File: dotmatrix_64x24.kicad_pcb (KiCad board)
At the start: 2 copper layers, 180 x 100 mm, 146 parts, among them CON1 BARREL_JACK, CON2 MRUSB-2B, P1 CONN_01X09, P2 CONN_01X09, P3 CONN_01X04, P4 CONN_01X03, P6 CONN_01X03, Q1 NJL7302L-F3, SW1 SW_PUSH_SMALL_H, SW2 SW_PUSH_SMALL_H, SW3 SW_PUSH_SMALL_H, SW4 SW_PUSH_SMALL_H, SW5 SW_PUSH_SMALL_H, SW6 SW_PUSH_SMALL_H, SW7 SW_PUSH_SMALL_H, SW8 SW_PUSH_SMALL_H, U1 WROOM-02, U10 LED1642GW, U11 LED1642GW, U12 AE-BME280, U13 OKL-T/6-W5, U14 NJU7223, U15 DS1307, U2 74HC595-alt-vdd, U3 TD62783, U4 74HC595-alt-vdd, U5 TD62783, U6 LED1642GW, U7 74HC595-alt-vdd, U8 TD62783, U9 LED1642GW, Y1 Crystal_Small

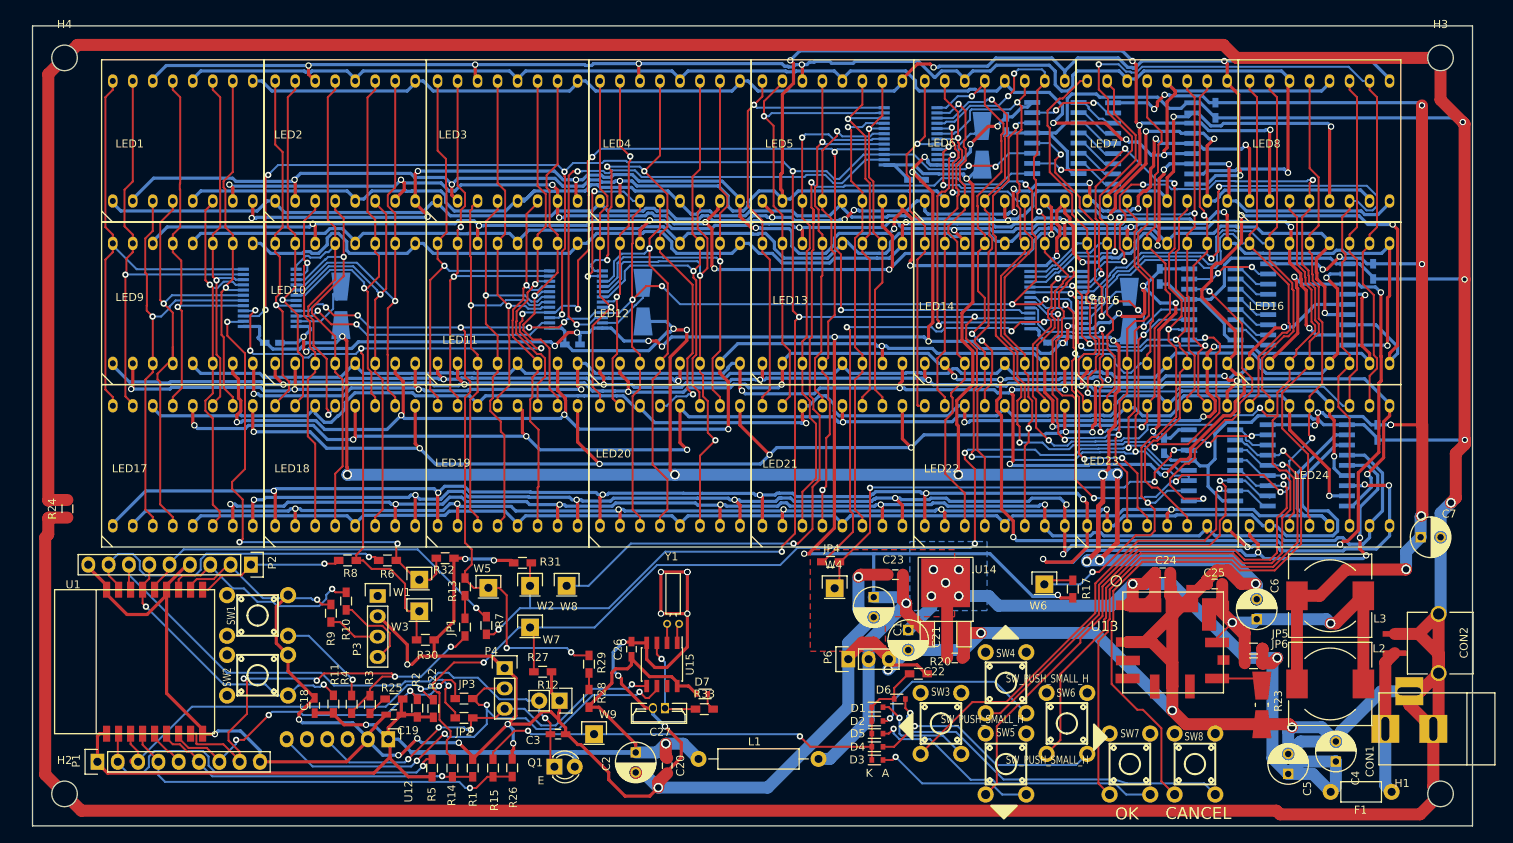
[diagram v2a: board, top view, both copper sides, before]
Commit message: Added CH340G USB-to-Serial chip
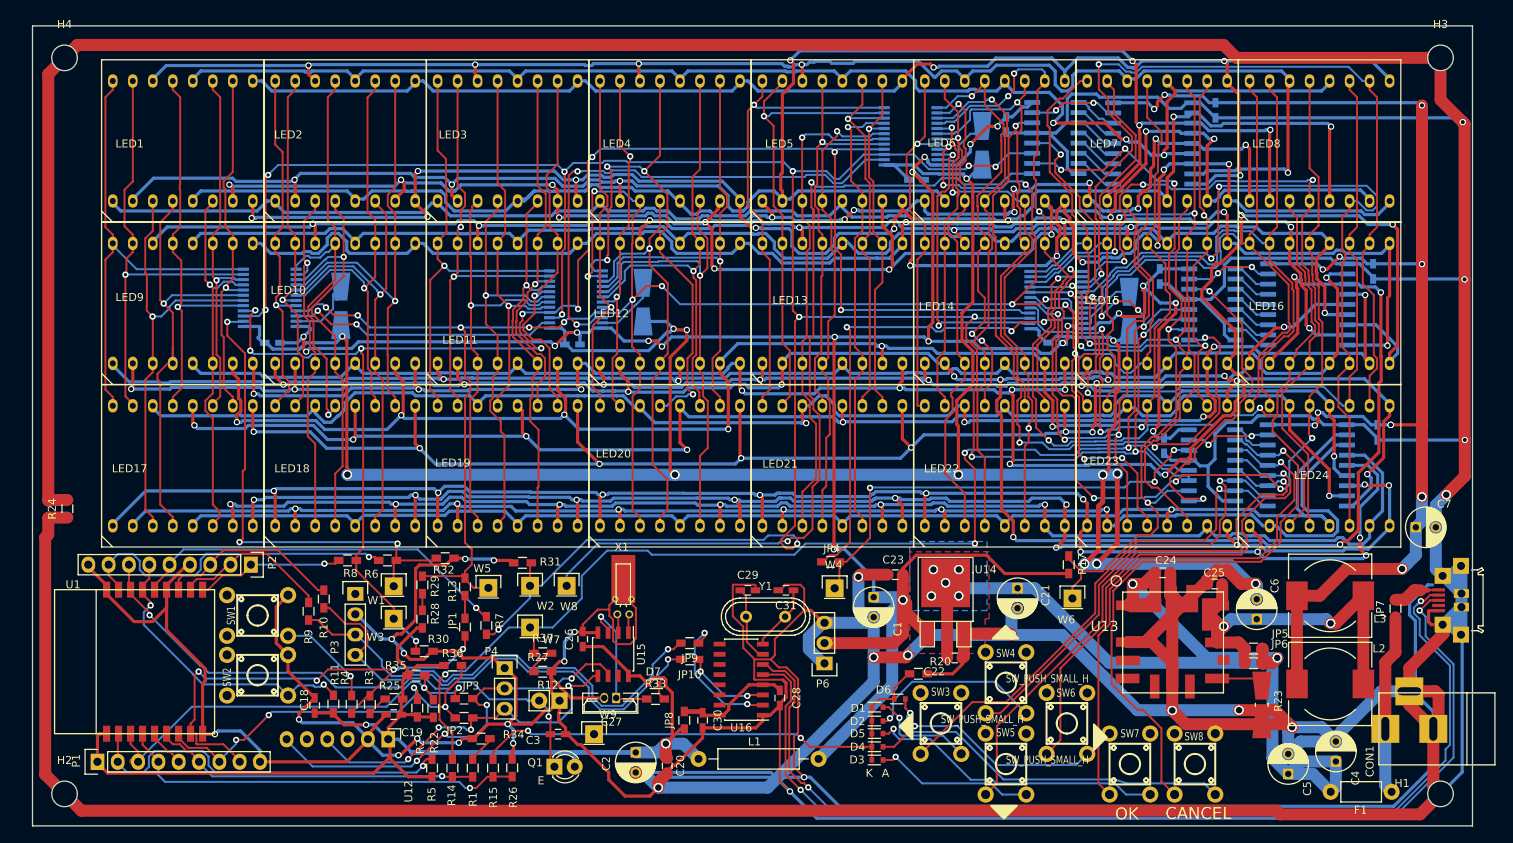
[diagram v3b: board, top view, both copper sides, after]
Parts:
- removed CON2: MRUSB-2B, components:MRUSB-2B
- added C28: 1u, Capacitors_SMD:C_0603_HandSoldering, F.Cu at (105.4, 96.0)
- added C29: 22p, Capacitors_SMD:C_0603_HandSoldering, F.Cu at (101.4, 82.5)
- added C30: 1u, Capacitors_SMD:C_0603_HandSoldering, F.Cu at (95.8, 98.8)
- added C31: 22p, Capacitors_SMD:C_0603_HandSoldering, F.Cu at (106.2, 82.5)
- added JP10: Jumper_NC_Small, Resistors_SMD:R_0603_HandSoldering, F.Cu at (94.2, 91.2)
- added JP7: Jumper_NC_Small, Resistors_SMD:R_0603_HandSoldering, F.Cu at (182.4, 84.8)
- added JP8: Jumper_NC_Small, Resistors_SMD:R_0603_HandSoldering, F.Cu at (93.5, 98.8)
- added JP9: Jumper_NC_Small, Resistors_SMD:R_0603_HandSoldering, F.Cu at (94.2, 89.2)
- added P5: USB_OTG, components:ZX62R-B-5P, F.Cu at (190.6, 83.8)
- added R34: 10k, Resistors_SMD:R_0603_HandSoldering, F.Cu at (68.1, 101.1)
- added R35: 10k, Resistors_SMD:R_0603_HandSoldering, F.Cu at (59.9, 93.2)
- added R36: 10k, Resistors_SMD:R_0603_HandSoldering, F.Cu at (64.5, 91.9)
- added R37: 10k, Resistors_SMD:R_0603_HandSoldering, F.Cu at (75.8, 90.4)
- added U16: CH340G, Housings_SOIC:SOIC-16_3.9x9.9mm_Pitch1.27mm, F.Cu at (100.6, 93.7)
- added X1: CRYSTAL_SMD, components:Crystal_Round_Horizontal_2mm_SHIELD, F.Cu at (85.9, 85.6)
- Y1: value Crystal_Small -> 12MHz; footprint Crystals:Crystal_Round_Horizontal_2mm -> Crystals:Crystal_HC49-U_Vertical
- moved R29 23.1 mm to (60.7, 81.9)
- moved R28 23.1 mm to (60.7, 86.2)
- moved C21 14.6 mm to (135.1, 82.3)
- moved Y1 11.6 mm to (103.6, 85.9)
- moved D7 6.23 mm to (89.6, 94.2)
- moved C27 6.23 mm to (85.0, 96.0)
- moved U15 6.23 mm to (84.6, 90.6)
- moved R33 6.23 mm to (89.9, 96.1)
- moved C26 6.23 mm to (80.8, 88.6)
- moved W6 3.92 mm to (142.0, 83.6)
- moved W3 3.33 mm to (57.1, 86.1)
- moved W1 3.30 mm to (57.1, 82.0)
- moved R17 3.09 mm to (141.5, 79.4)
- moved P6 3.02 mm to (111.0, 91.7), turned to 180 degrees
- moved P3 2.81 mm to (52.3, 83.0)
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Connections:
- net Net-(P3-Pad3) renamed /RXD
- net Net-(P3-Pad4) renamed /TXD
- P1 pad 3: Net-(JP2-Pad1) -> Net-(JP3-Pad1)
- P1 pad 7: Net-(JP3-Pad1) -> Net-(JP2-Pad1)
- R1 pad 1: GND -> Net-(R1-Pad1)
- R2 pad 2: Net-(JP3-Pad1) -> Net-(JP2-Pad1)
- R22 pad 2: Net-(JP2-Pad1) -> Net-(JP3-Pad1)
- R27 pad 1: /Sheet57A04605/HC595LATCH -> Net-(R27-Pad1)
- U1 pad 3: Net-(JP2-Pad1) -> Net-(JP3-Pad1)
- U1 pad 7: Net-(JP3-Pad1) -> Net-(JP2-Pad1)
- Y1 pad 1: Net-(U15-Pad2) -> Net-(C29-Pad1)
- Y1 pad 2: Net-(U15-Pad1) -> Net-(C31-Pad1)
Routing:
- net GND: track 1520.8 -> 1896.1 mm, vias 41 -> 40
- net /USB_DM: track 0.00 -> 128.0 mm, vias 0 -> 2
- net /USB_DP: track 0.00 -> 127.3 mm, vias 0 -> 2
- net /RXD: track 6.60 -> 59.5 mm, vias 0 -> 1
- net /TXD: track 10.3 -> 60.9 mm, vias 0 -> 1
- net VCC: track 119.9 -> 140.0 mm
- net Net-(JP9-Pad1): track 0.00 -> 17.4 mm, vias 0 -> 2
- net /Sheet57A04605/COLPWCLK: track 195.1 -> 180.6 mm, vias 14 -> 12
- net Net-(C28-Pad1): track 0.00 -> 14.3 mm
- net /ESPVDD: track 144.1 -> 157.1 mm
- net /Sheet57A04605/r21: track 220.3 -> 209.1 mm
- net Net-(JP10-Pad1): track 0.00 -> 10.7 mm, vias 0 -> 2
- net /SCL: track 64.2 -> 53.7 mm
- net Net-(C29-Pad1): track 0.00 -> 9.43 mm
- net Net-(JP3-Pad1): track 44.6 -> 54.0 mm, vias 4 -> 2
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
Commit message: filled copper zones, placed via stitching ... etc.
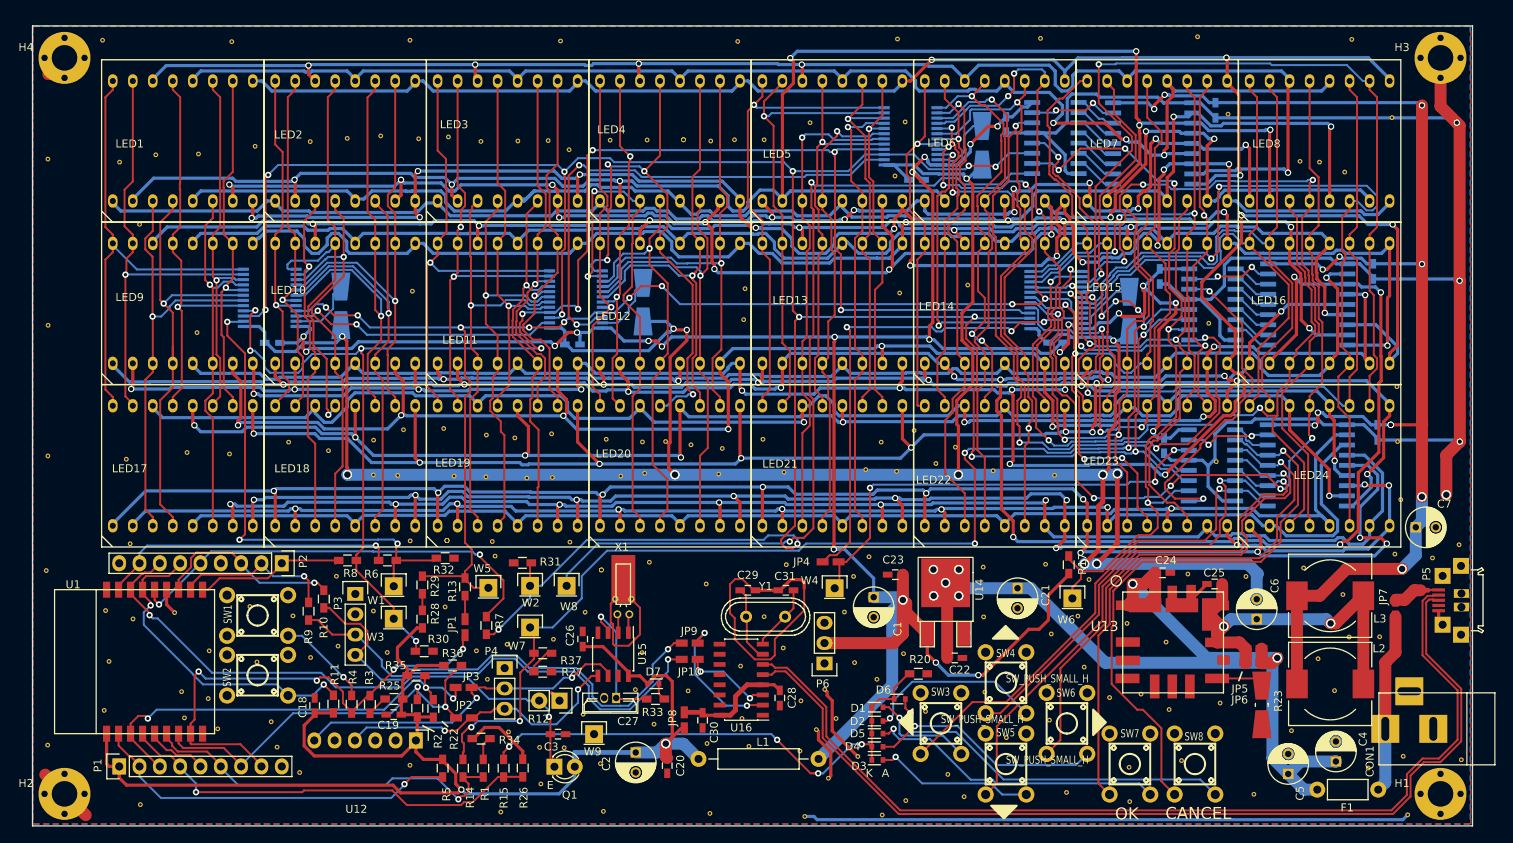
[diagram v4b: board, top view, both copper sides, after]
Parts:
- removed R24: 120R, Resistors_SMD:R_0603_HandSoldering
- added REF**: stitch-via-0.6mm, components:stitch-via-0.6mm, F.Cu at (108.1, 96.4)
- added REF**: stitch-via-0.6mm, components:stitch-via-0.6mm, F.Cu at (116.2, 67.5)
- added REF**: stitch-via-0.6mm, components:stitch-via-0.6mm, F.Cu at (71.5, 100.3)
- added REF**: stitch-via-0.6mm, components:stitch-via-0.6mm, F.Cu at (68.9, 93.7)
- added REF**: stitch-via-0.6mm, components:stitch-via-0.6mm, F.Cu at (54.6, 85.1)
- added REF**: stitch-via-0.6mm, components:stitch-via-0.6mm, F.Cu at (50.0, 80.8)
- added REF**: stitch-via-0.6mm, components:stitch-via-0.6mm, F.Cu at (50.2, 89.5)
- added REF**: stitch-via-0.6mm, components:stitch-via-0.6mm, F.Cu at (46.8, 91.0)
- added REF**: stitch-via-0.6mm, components:stitch-via-0.6mm, F.Cu at (59.2, 104.4)
- added REF**: stitch-via-0.6mm, components:stitch-via-0.6mm, F.Cu at (45.4, 105.3)
- added REF**: stitch-via-0.6mm, components:stitch-via-0.6mm, F.Cu at (42.6, 102.2)
- added REF**: stitch-via-0.6mm, components:stitch-via-0.6mm, F.Cu at (41.8, 99.0)
- added REF**: stitch-via-0.6mm, components:stitch-via-0.6mm, F.Cu at (105.9, 67.8)
- added REF**: stitch-via-0.6mm, components:stitch-via-0.6mm, F.Cu at (35.2, 99.9)
- added REF**: stitch-via-0.6mm, components:stitch-via-0.6mm, F.Cu at (39.2, 84.6)
- added REF**: stitch-via-0.6mm, components:stitch-via-0.6mm, F.Cu at (29.8, 85.3)
- added REF**: stitch-via-0.6mm, components:stitch-via-0.6mm, F.Cu at (21.0, 97.6)
- added REF**: stitch-via-0.6mm, components:stitch-via-0.6mm, F.Cu at (21.1, 85.1)
- added REF**: stitch-via-0.6mm, components:stitch-via-0.6mm, F.Cu at (13.9, 101.9)
- added REF**: stitch-via-0.6mm, components:stitch-via-0.6mm, F.Cu at (159.0, 49.2)
- added REF**: stitch-via-0.6mm, components:stitch-via-0.6mm, F.Cu at (160.0, 66.5)
- added REF**: stitch-via-0.6mm, components:stitch-via-0.6mm, F.Cu at (120.0, 67.7)
- added REF**: stitch-via-0.6mm, components:stitch-via-0.6mm, F.Cu at (122.2, 62.6)
- added REF**: stitch-via-0.6mm, components:stitch-via-0.6mm, F.Cu at (97.8, 68.0)
- added REF**: stitch-via-0.6mm, components:stitch-via-0.6mm, F.Cu at (128.9, 44.4)
- added REF**: stitch-via-0.6mm, components:stitch-via-0.6mm, F.Cu at (100.9, 48.7)
- added REF**: stitch-via-0.6mm, components:stitch-via-0.6mm, F.Cu at (103.5, 26.2)
- added REF**: stitch-via-0.6mm, components:stitch-via-0.6mm, F.Cu at (99.7, 26.2)
- added REF**: stitch-via-0.6mm, components:stitch-via-0.6mm, F.Cu at (96.8, 26.4)
- added REF** (x2): stitch-via-0.6mm, components:stitch-via-0.6mm, F.Cu at (93.4, 26.2)
- added REF**: stitch-via-0.6mm, components:stitch-via-0.6mm, F.Cu at (88.8, 26.3)
- added REF**: stitch-via-0.6mm, components:stitch-via-0.6mm, F.Cu at (84.2, 26.3)
- added REF**: stitch-via-0.6mm, components:stitch-via-0.6mm, F.Cu at (79.1, 27.5)
- added REF**: stitch-via-0.6mm, components:stitch-via-0.6mm, F.Cu at (88.5, 67.9)
- added REF**: stitch-via-0.6mm, components:stitch-via-0.6mm, F.Cu at (76.5, 26.3)
- added REF**: stitch-via-0.6mm, components:stitch-via-0.6mm, F.Cu at (72.7, 26.4)
- added REF**: stitch-via-0.6mm, components:stitch-via-0.6mm, F.Cu at (68.0, 26.4)
- added REF**: stitch-via-0.6mm, components:stitch-via-0.6mm, F.Cu at (64.0, 25.9)
- added REF**: stitch-via-0.6mm, components:stitch-via-0.6mm, F.Cu at (60.3, 26.1)
- added REF**: stitch-via-0.6mm, components:stitch-via-0.6mm, F.Cu at (55.5, 25.8)
- added REF**: stitch-via-0.6mm, components:stitch-via-0.6mm, F.Cu at (51.3, 26.1)
- added REF**: stitch-via-0.6mm, components:stitch-via-0.6mm, F.Cu at (46.7, 26.5)
- added REF**: stitch-via-0.6mm, components:stitch-via-0.6mm, F.Cu at (39.8, 27.1)
- added REF**: stitch-via-0.6mm, components:stitch-via-0.6mm, F.Cu at (32.7, 28.0)
- added REF**: stitch-via-0.6mm, components:stitch-via-0.6mm, F.Cu at (85.5, 68.3)
- added REF**: stitch-via-0.6mm, components:stitch-via-0.6mm, F.Cu at (27.4, 28.1)
- added REF**: stitch-via-0.6mm, components:stitch-via-0.6mm, F.Cu at (22.9, 29.0)
- added REF**: stitch-via-0.6mm, components:stitch-via-0.6mm, F.Cu at (25.4, 36.8)
- added REF**: stitch-via-0.6mm, components:stitch-via-0.6mm, F.Cu at (32.6, 50.3)
- added REF**: stitch-via-0.6mm, components:stitch-via-0.6mm, F.Cu at (23.7, 66.2)
- added REF**: stitch-via-0.6mm, components:stitch-via-0.6mm, F.Cu at (31.3, 65.3)
- added REF**: stitch-via-0.6mm, components:stitch-via-0.6mm, F.Cu at (36.6, 65.5)
- added REF**: stitch-via-0.6mm, components:stitch-via-0.6mm, F.Cu at (44.0, 64.0)
- added REF**: stitch-via-0.6mm, components:stitch-via-0.6mm, F.Cu at (49.0, 65.1)
- added REF**: stitch-via-0.6mm, components:stitch-via-0.6mm, F.Cu at (54.6, 63.8)
- added REF**: stitch-via-0.6mm, components:stitch-via-0.6mm, F.Cu at (77.0, 68.5)
- added REF**: stitch-via-0.6mm, components:stitch-via-0.6mm, F.Cu at (58.4, 62.5)
- added REF**: stitch-via-0.6mm, components:stitch-via-0.6mm, F.Cu at (63.4, 62.3)
- added REF**: stitch-via-0.6mm, components:stitch-via-0.6mm, F.Cu at (68.7, 63.1)
- added REF**: stitch-via-0.6mm, components:stitch-via-0.6mm, F.Cu at (72.3, 63.5)
- added REF**: stitch-via-0.6mm, components:stitch-via-0.6mm, F.Cu at (76.9, 63.0)
- added REF**: stitch-via-0.6mm, components:stitch-via-0.6mm, F.Cu at (83.7, 63.7)
- added REF**: stitch-via-0.6mm, components:stitch-via-0.6mm, F.Cu at (88.2, 64.0)
- added REF**: stitch-via-0.6mm, components:stitch-via-0.6mm, F.Cu at (91.1, 64.0)
- added REF**: stitch-via-0.6mm, components:stitch-via-0.6mm, F.Cu at (94.3, 64.4)
- added REF**: stitch-via-0.6mm, components:stitch-via-0.6mm, F.Cu at (98.2, 64.8)
- added REF**: stitch-via-0.6mm, components:stitch-via-0.6mm, F.Cu at (73.8, 68.5)
- added REF**: stitch-via-0.6mm, components:stitch-via-0.6mm, F.Cu at (103.3, 63.7)
- added REF**: stitch-via-0.6mm, components:stitch-via-0.6mm, F.Cu at (118.1, 64.0)
- added REF**: stitch-via-0.6mm, components:stitch-via-0.6mm, F.Cu at (120.4, 45.4)
- added REF**: stitch-via-0.6mm, components:stitch-via-0.6mm, F.Cu at (101.1, 44.9)
- added REF**: stitch-via-0.6mm, components:stitch-via-0.6mm, F.Cu at (59.5, 45.2)
- added REF**: stitch-via-0.6mm, components:stitch-via-0.6mm, F.Cu at (109.2, 24.1)
- added REF**: stitch-via-0.6mm, components:stitch-via-0.6mm, F.Cu at (119.8, 30.8)
- added REF**: stitch-via-0.6mm, components:stitch-via-0.6mm, F.Cu at (170.4, 28.9)
- added REF**: stitch-via-0.6mm, components:stitch-via-0.6mm, F.Cu at (161.4, 23.0)
- added REF**: stitch-via-0.6mm, components:stitch-via-0.6mm, F.Cu at (176.0, 30.3)
- added REF**: stitch-via-0.6mm, components:stitch-via-0.6mm, F.Cu at (68.7, 68.4)
- added REF**: stitch-via-0.6mm, components:stitch-via-0.6mm, F.Cu at (172.9, 29.0)
- added REF**: stitch-via-0.6mm, components:stitch-via-0.6mm, F.Cu at (181.9, 23.5)
- added REF**: stitch-via-0.6mm, components:stitch-via-0.6mm, F.Cu at (182.5, 57.1)
- added REF**: stitch-via-0.6mm, components:stitch-via-0.6mm, F.Cu at (182.6, 64.0)
- added REF**: stitch-via-0.6mm, components:stitch-via-0.6mm, F.Cu at (183.0, 71.2)
- added REF**: stitch-via-0.6mm, components:stitch-via-0.6mm, F.Cu at (187.0, 78.5)
- added REF**: stitch-via-0.6mm, components:stitch-via-0.6mm, F.Cu at (190.3, 76.9)
- added REF**: stitch-via-0.6mm, components:stitch-via-0.6mm, F.Cu at (175.8, 83.1)
- added REF**: stitch-via-0.6mm, components:stitch-via-0.6mm, F.Cu at (176.6, 88.4)
- added REF**: stitch-via-0.6mm, components:stitch-via-0.6mm, F.Cu at (183.3, 103.3)
- added REF**: stitch-via-0.6mm, components:stitch-via-0.6mm, F.Cu at (64.7, 68.3)
- added REF**: stitch-via-0.6mm, components:stitch-via-0.6mm, F.Cu at (190.6, 103.7)
- added REF**: stitch-via-0.6mm, components:stitch-via-0.6mm, F.Cu at (183.9, 110.6)
- added REF**: stitch-via-0.6mm, components:stitch-via-0.6mm, F.Cu at (176.9, 13.7)
- added REF**: stitch-via-0.6mm, components:stitch-via-0.6mm, F.Cu at (157.6, 13.4)
- added REF**: stitch-via-0.6mm, components:stitch-via-0.6mm, F.Cu at (138.0, 13.6)
- added REF**: stitch-via-0.6mm, components:stitch-via-0.6mm, F.Cu at (120.1, 13.6)
- added REF**: stitch-via-0.6mm, components:stitch-via-0.6mm, F.Cu at (100.2, 13.9)
- added REF**: stitch-via-0.6mm, components:stitch-via-0.6mm, F.Cu at (78.0, 13.9)
- added REF**: stitch-via-0.6mm, components:stitch-via-0.6mm, F.Cu at (59.2, 13.8)
- added REF**: stitch-via-0.6mm, components:stitch-via-0.6mm, F.Cu at (36.9, 14.0)
- added REF**: stitch-via-0.6mm, components:stitch-via-0.6mm, F.Cu at (54.6, 68.1)
- added REF**: stitch-via-0.6mm, components:stitch-via-0.6mm, F.Cu at (20.8, 13.8)
- added REF**: stitch-via-0.6mm, components:stitch-via-0.6mm, F.Cu at (13.9, 28.7)
- added REF**: stitch-via-0.6mm, components:stitch-via-0.6mm, F.Cu at (13.9, 49.4)
- added REF**: stitch-via-0.6mm, components:stitch-via-0.6mm, F.Cu at (13.9, 65.8)
- added REF**: stitch-via-0.6mm, components:stitch-via-0.6mm, F.Cu at (59.2, 76.4)
- added REF**: stitch-via-0.6mm, components:stitch-via-0.6mm, F.Cu at (25.5, 109.3)
- added REF**: stitch-via-0.6mm, components:stitch-via-0.6mm, F.Cu at (13.7, 80.1)
- added REF**: stitch-via-0.6mm, components:stitch-via-0.6mm, F.Cu at (44.6, 85.8)
- added REF**: stitch-via-0.6mm, components:stitch-via-0.6mm, F.Cu at (63.6, 84.6)
- added REF** (x2): stitch-via-0.6mm, components:stitch-via-0.6mm, F.Cu at (83.1, 80.0)
- added REF**: stitch-via-0.6mm, components:stitch-via-0.6mm, F.Cu at (141.2, 107.8)
- added REF**: stitch-via-0.6mm, components:stitch-via-0.6mm, F.Cu at (57.7, 68.2)
- added REF**: stitch-via-0.6mm, components:stitch-via-0.6mm, F.Cu at (89.1, 79.0)
- added REF**: stitch-via-0.6mm, components:stitch-via-0.6mm, F.Cu at (69.8, 78.3)
- added REF**: stitch-via-0.6mm, components:stitch-via-0.6mm, F.Cu at (69.5, 76.5)
- added REF** (x3): stitch-via-0.6mm, components:stitch-via-0.6mm, F.Cu at (63.8, 76.3)
- added REF**: stitch-via-0.6mm, components:stitch-via-0.6mm, F.Cu at (182.3, 78.0)
- added REF**: stitch-via-0.6mm, components:stitch-via-0.6mm, F.Cu at (174.8, 95.1)
- added REF**: stitch-via-0.6mm, components:stitch-via-0.6mm, F.Cu at (179.0, 104.8)
- added REF**: stitch-via-0.6mm, components:stitch-via-0.6mm, F.Cu at (150.6, 95.5)
- added REF**: stitch-via-0.6mm, components:stitch-via-0.6mm, F.Cu at (146.6, 96.0)
- added REF**: stitch-via-0.6mm, components:stitch-via-0.6mm, F.Cu at (156.4, 80.5)
- added REF**: stitch-via-0.6mm, components:stitch-via-0.6mm, F.Cu at (148.8, 86.7)
- added REF**: stitch-via-0.6mm, components:stitch-via-0.6mm, F.Cu at (142.7, 85.8)
- added REF**: stitch-via-0.6mm, components:stitch-via-0.6mm, F.Cu at (139.8, 68.2)
- added REF**: stitch-via-0.6mm, components:stitch-via-0.6mm, F.Cu at (149.1, 109.0)
- added REF**: stitch-via-0.6mm, components:stitch-via-0.6mm, F.Cu at (114.6, 80.8)
- added REF**: stitch-via-0.6mm, components:stitch-via-0.6mm, F.Cu at (107.9, 102.6)
- added REF**: stitch-via-0.6mm, components:stitch-via-0.6mm, F.Cu at (96.7, 110.4)
- added REF**: stitch-via-0.6mm, components:stitch-via-0.6mm, F.Cu at (96.3, 101.7)
- added REF**: stitch-via-0.6mm, components:stitch-via-0.6mm, F.Cu at (83.0, 104.2)
- added REF**: stitch-via-0.6mm, components:stitch-via-0.6mm, F.Cu at (79.2, 76.5)
- added REF**: stitch-via-0.6mm, components:stitch-via-0.6mm, F.Cu at (56.3, 90.3)
- added REF**: stitch-via-0.6mm, components:stitch-via-0.6mm, F.Cu at (31.0, 98.5)
- added REF**: stitch-via-0.6mm, components:stitch-via-0.6mm, F.Cu at (34.1, 90.1)
- added REF**: stitch-via-0.6mm, components:stitch-via-0.6mm, F.Cu at (24.6, 86.1)
- added REF**: stitch-via-0.6mm, components:stitch-via-0.6mm, F.Cu at (118.2, 110.6)
- added REF**: stitch-via-0.6mm, components:stitch-via-0.6mm, F.Cu at (24.2, 76.7)
- added REF**: stitch-via-0.6mm, components:stitch-via-0.6mm, F.Cu at (87.4, 95.0)
- added REF**: stitch-via-0.6mm, components:stitch-via-0.6mm, F.Cu at (71.3, 89.3)
- added REF**: stitch-via-0.6mm, components:stitch-via-0.6mm, F.Cu at (77.1, 88.7)
- added REF**: stitch-via-0.6mm, components:stitch-via-0.6mm, F.Cu at (81.1, 85.3)
- added REF**: stitch-via-0.6mm, components:stitch-via-0.6mm, F.Cu at (67.5, 90.1)
- added REF**: stitch-via-0.6mm, components:stitch-via-0.6mm, F.Cu at (103.5, 85.9)
- added REF**: stitch-via-0.6mm, components:stitch-via-0.6mm, F.Cu at (121.1, 24.0)
- added REF**: stitch-via-0.6mm, components:stitch-via-0.6mm, F.Cu at (40.1, 91.5)
- added REF**: stitch-via-0.6mm, components:stitch-via-0.6mm, F.Cu at (34.0, 96.1)
- added REF**: stitch-via-0.6mm, components:stitch-via-0.6mm, F.Cu at (121.2, 108.8)
- added REF**: stitch-via-0.6mm, components:stitch-via-0.6mm, F.Cu at (30.6, 95.2)
- added REF**: stitch-via-0.6mm, components:stitch-via-0.6mm, F.Cu at (21.6, 91.4)
- added REF**: stitch-via-0.6mm, components:stitch-via-0.6mm, F.Cu at (117.6, 93.7)
- added REF**: stitch-via-0.6mm, components:stitch-via-0.6mm, F.Cu at (155.6, 103.8)
- added REF**: stitch-via-0.6mm, components:stitch-via-0.6mm, F.Cu at (170.9, 79.8)
- added REF**: stitch-via-0.6mm, components:stitch-via-0.6mm, F.Cu at (169.4, 100.1)
- added REF**: stitch-via-0.6mm, components:stitch-via-0.6mm, F.Cu at (172.7, 91.1)
- added REF**: stitch-via-0.6mm, components:stitch-via-0.6mm, F.Cu at (180.4, 88.4)
- added REF**: stitch-via-0.6mm, components:stitch-via-0.6mm, F.Cu at (163.7, 80.8)
- added REF**: stitch-via-0.6mm, components:stitch-via-0.6mm, F.Cu at (153.7, 89.0)
- added REF**: stitch-via-0.6mm, components:stitch-via-0.6mm, F.Cu at (112.4, 98.6)
- added REF**: stitch-via-0.6mm, components:stitch-via-0.6mm, F.Cu at (143.5, 92.2)
- added REF**: stitch-via-0.6mm, components:stitch-via-0.6mm, F.Cu at (160.5, 96.6)
- added REF**: stitch-via-0.6mm, components:stitch-via-0.6mm, F.Cu at (154.1, 97.5)
- added REF**: stitch-via-0.6mm, components:stitch-via-0.6mm, F.Cu at (164.7, 108.1)
- added REF**: stitch-via-0.6mm, components:stitch-via-0.6mm, F.Cu at (149.1, 104.7)
- added REF**: stitch-via-0.6mm, components:stitch-via-0.6mm, F.Cu at (133.7, 101.0)
- added REF**: stitch-via-0.6mm, components:stitch-via-0.6mm, F.Cu at (139.1, 98.8)
- added REF**: stitch-via-0.6mm, components:stitch-via-0.6mm, F.Cu at (131.0, 95.3)
- added REF**: stitch-via-0.6mm, components:stitch-via-0.6mm, F.Cu at (139.3, 88.0)
- added REF**: stitch-via-0.6mm, components:stitch-via-0.6mm, F.Cu at (144.1, 81.2)
- added REF**: stitch-via-0.6mm, components:stitch-via-0.6mm, F.Cu at (132.1, 67.6)
- added REF**: stitch-via-0.6mm, components:stitch-via-0.6mm, F.Cu at (138.6, 79.3)
- added REF**: stitch-via-0.6mm, components:stitch-via-0.6mm, F.Cu at (130.8, 79.7)
- added REF**: stitch-via-0.6mm, components:stitch-via-0.6mm, F.Cu at (130.9, 85.9)
- added REF**: stitch-via-0.6mm, components:stitch-via-0.6mm, F.Cu at (114.8, 91.6)
- added REF**: stitch-via-0.6mm, components:stitch-via-0.6mm, F.Cu at (116.6, 78.4)
- added REF**: stitch-via-0.6mm, components:stitch-via-0.6mm, F.Cu at (120.9, 90.5)
- added REF**: stitch-via-0.6mm, components:stitch-via-0.6mm, F.Cu at (123.6, 97.7)
- added REF**: stitch-via-0.6mm, components:stitch-via-0.6mm, F.Cu at (126.4, 105.6)
- added REF**: stitch-via-0.6mm, components:stitch-via-0.6mm, F.Cu at (128.4, 108.4)
- added REF**: stitch-via-0.6mm, components:stitch-via-0.6mm, F.Cu at (115.2, 103.3)
- added REF**: stitch-via-0.6mm, components:stitch-via-0.6mm, F.Cu at (127.4, 64.7)
- added REF**: stitch-via-0.6mm, components:stitch-via-0.6mm, F.Cu at (111.5, 106.0)
- added REF**: stitch-via-0.6mm, components:stitch-via-0.6mm, F.Cu at (101.5, 102.1)
- added REF**: stitch-via-0.6mm, components:stitch-via-0.6mm, F.Cu at (100.7, 98.6)
- added REF**: stitch-via-0.6mm, components:stitch-via-0.6mm, F.Cu at (110.0, 100.0)
- added REF**: stitch-via-0.6mm, components:stitch-via-0.6mm, F.Cu at (111.0, 94.9)
- added REF**: stitch-via-0.6mm, components:stitch-via-0.6mm, F.Cu at (113.5, 85.3)
- added REF**: stitch-via-0.6mm, components:stitch-via-0.6mm, F.Cu at (100.5, 92.0)
- added REF**: stitch-via-0.6mm, components:stitch-via-0.6mm, F.Cu at (105.8, 89.8)
- added REF**: stitch-via-0.6mm, components:stitch-via-0.6mm, F.Cu at (106.2, 79.3)
- added REF**: stitch-via-0.6mm, components:stitch-via-0.6mm, F.Cu at (96.2, 81.8)
- added REF**: stitch-via-0.6mm, components:stitch-via-0.6mm, F.Cu at (124.9, 66.7)
- added REF**: stitch-via-0.6mm, components:stitch-via-0.6mm, F.Cu at (88.2, 90.3)
- added REF**: stitch-via-0.6mm, components:stitch-via-0.6mm, F.Cu at (94.0, 95.1)
- added REF**: stitch-via-0.6mm, components:stitch-via-0.6mm, F.Cu at (89.7, 99.3)
- added REF**: stitch-via-0.6mm, components:stitch-via-0.6mm, F.Cu at (80.8, 98.0)
- added REF**: stitch-via-0.6mm, components:stitch-via-0.6mm, F.Cu at (108.5, 110.8)
- added REF**: stitch-via-0.6mm, components:stitch-via-0.6mm, F.Cu at (83.4, 110.2)
- added REF**: stitch-via-0.6mm, components:stitch-via-0.6mm, F.Cu at (70.5, 110.3)
- added REF**: stitch-via-0.6mm, components:stitch-via-0.6mm, F.Cu at (75.5, 106.8)
- added REF**: stitch-via-0.6mm, components:stitch-via-0.6mm, F.Cu at (78.5, 102.2)
- added REF**: stitch-via-0.6mm, components:stitch-via-0.6mm, F.Cu at (75.4, 102.2)
- H1, H2, H3, H4: footprint Mounting_Holes:MountingHole_3.2mm_M3 -> components:MountingHole_3.2mm_M3
- JP1, JP10, JP2, JP3, JP4, JP5, JP6, JP7, JP8, JP9: footprint Resistors_SMD:R_0603_HandSoldering -> components:SolderJumper
- moved P2 3.86 mm to (43.2, 79.2)
- moved U12 3.46 mm to (59.9, 101.3)
- moved P1 2.78 mm to (22.8, 104.6)
- moved F1 1.70 mm to (180.2, 107.5)
- moved JP3 1.40 mm to (65.9, 94.7)
- moved R1 1.32 mm to (68.3, 104.8)
- moved R5 1.32 mm to (63.3, 104.8), turned to 270 degrees
- moved R14 1.32 mm to (65.8, 104.8)
- moved R15 1.32 mm to (70.9, 104.8)
- moved R26 1.32 mm to (73.3, 104.8)
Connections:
- net /USB_DM renamed /USB_D_N
- net /USB_DP renamed /USB_D_P
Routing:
- net GND: track 1896.1 -> 731.9 mm, vias 40 -> 16
- net VCC: track 140.0 -> 155.4 mm
- net /ESPVDD: track 157.1 -> 171.0 mm
- net /SCL: track 53.7 -> 44.1 mm, vias 4 -> 2
- net /LEDLOGICVDD: track 315.0 -> 323.0 mm, vias 20 -> 22
- net /SDA: track 44.5 -> 36.9 mm, vias 4 -> 2
- net Net-(P2-Pad5): track 48.8 -> 55.9 mm, vias 1 -> 2
- net Net-(P1-Pad6): track 41.2 -> 47.6 mm
- net /Sheet57A04605/r21: track 209.1 -> 215.1 mm
- net /Sheet57A04605/HC595LATCH: track 190.9 -> 185.9 mm, vias 9 -> 10
- net /Sheet57A04605/c14: track 53.7 -> 58.3 mm
- net Net-(P2-Pad8): track 42.2 -> 37.7 mm
- net /USB_D_N: track 128.0 -> 123.7 mm, vias 2 -> 0
- net /USB_D_P: track 127.3 -> 123.2 mm, vias 2 -> 0
- net Net-(P2-Pad6): track 37.5 -> 41.2 mm
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- added copper zone on B.Cu, net GND
- added copper zone on F.Cu, net GND
- removed copper zone on B.Cu, net VCC
- removed copper zone on F.Cu, net VCC

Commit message: Ground plane fix, XTAL footprint fix
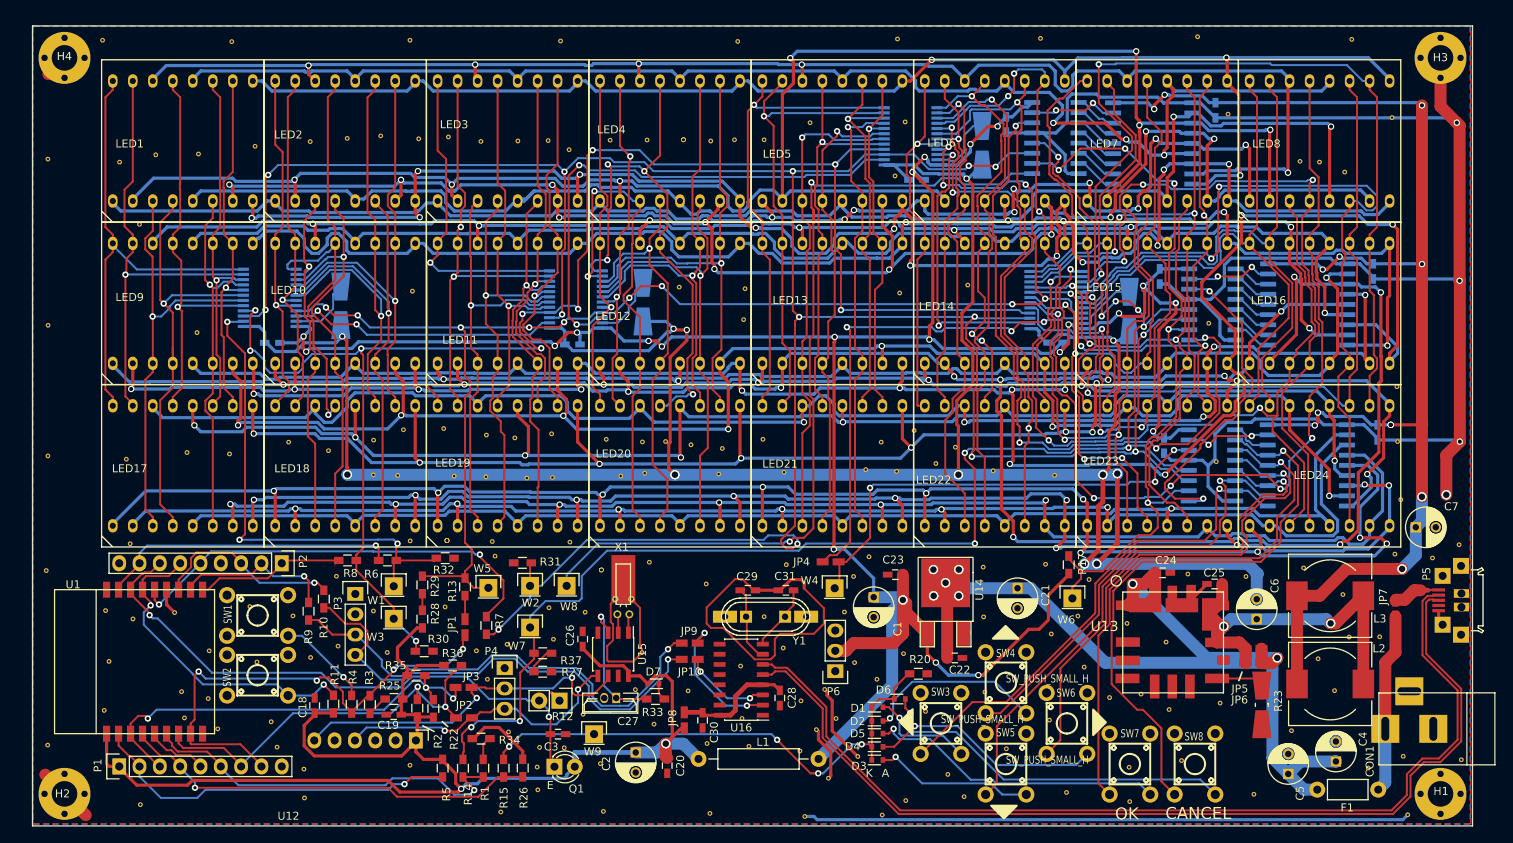
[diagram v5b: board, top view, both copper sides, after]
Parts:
- added REF**: stitch-via-0.6mm, components:stitch-via-0.6mm, F.Cu at (75.1, 104.6)
- added REF**: stitch-via-0.6mm, components:stitch-via-0.6mm, F.Cu at (46.0, 108.5)
- added REF**: stitch-via-0.6mm, components:stitch-via-0.6mm, F.Cu at (92.8, 44.7)
- added REF**: stitch-via-0.6mm, components:stitch-via-0.6mm, F.Cu at (76.6, 84.7)
- Y1: footprint Crystals:Crystal_HC49-U_Vertical -> components:Crystal_HC49-U_Vertical_SMD_Universal
- moved P6 1.66 mm to (112.3, 92.7)
- moved REF** 1.40 mm to (133.7, 102.4)
- moved REF** 0.83 mm to (75.2, 107.5)
- moved REF** 0.69 mm to (45.9, 104.9)
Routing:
- net GND: track 731.9 -> 744.1 mm
- net /ESPVDD: track 171.0 -> 169.7 mm
- net Net-(P1-Pad4): track 54.5 -> 53.2 mm
- net /SCL: track 44.1 -> 45.2 mm
- net /LEDLOGICVDD: track 323.0 -> 322.0 mm
- net /Sheet57A04605/HC595LATCH: track 185.9 -> 186.7 mm
